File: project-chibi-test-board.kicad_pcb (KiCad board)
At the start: 4 copper layers, 104.1 x 134.6 mm, 221 parts, among them J1 Conn_01x04, J10 Conn_01x02, J11 Conn_01x02, J12 Conn_02x06_Top_Bottom, J13 Conn_02x06_Top_Bottom, J14 Conn_02x06_Top_Bottom, J15 Conn_02x06_Top_Bottom, J16 Conn_01x02, J17 Conn_01x02, J18 Conn_Coaxial, J19 Conn_Coaxial, J2 Conn_Coaxial, J20 Conn_01x03, J21 Conn_01x03, J22 Conn_01x04, J23 USB_B_Micro, J24 Conn_01x06, J25 Conn_01x04, J26 Conn_Coaxial, J27 Conn_Coaxial, J28 Conn_01x03, J29 Conn_01x03, J3 Conn_Coaxial, J30 Conn_01x02, J31 Conn_01x02, J32 Conn_02x06_Top_Bottom, J33 Conn_02x06_Top_Bottom, J34 Conn_02x06_Top_Bottom, J35 Conn_02x06_Top_Bottom, J36 Conn_02x06_Top_Bottom, J37 Conn_02x06_Top_Bottom, J38 Conn_02x06_Top_Bottom, J39 Conn_02x06_Top_Bottom, J4 Conn_01x03, J40 Conn_01x02, J41 Conn_01x02, J42 Conn_Coaxial, J43 Conn_Coaxial, J44 Conn_01x04, J45 Conn_01x03, J46 Conn_01x03, J47 Conn_01x06, J5 Conn_01x03, J6 Conn_02x06_Top_Bottom, J7 Conn_02x06_Top_Bottom, J8 Conn_02x06_Top_Bottom, J9 Conn_01x06, SW1 SW_DIP_x08, SW2 SW_DIP_x08, U1 40 MHz, U10 5M240ZT144C5N, U11 5M1270ZF256C5N, U2 2.048 MHz, U3 5M40ZE64C5N, U4 5M2210ZF256C5N, U5 93LC56BT-OT, U6 5M240ZT144C5N, U7 LM1117-3.3, U8 LM1117-1.8, U9 FT232H, Y1 12 MHz

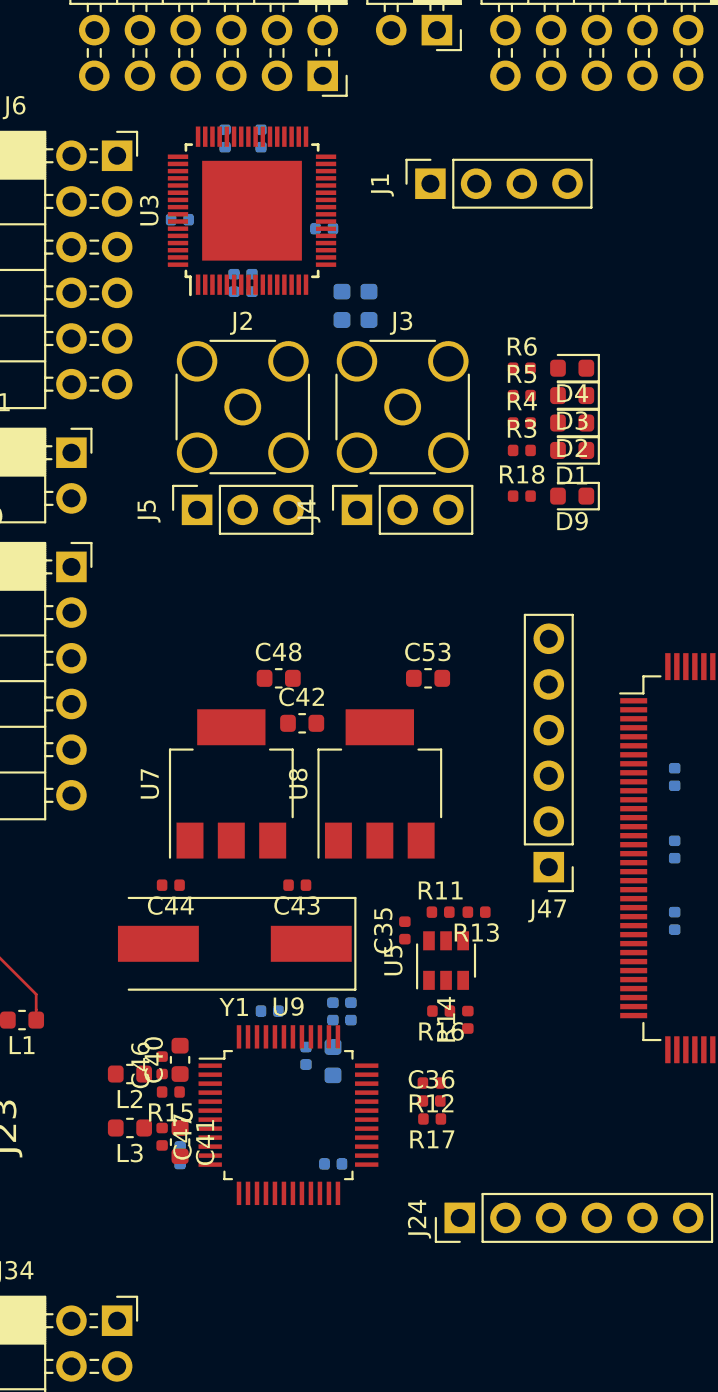
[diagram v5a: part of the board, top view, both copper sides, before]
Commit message: clean up 40z pin ordering
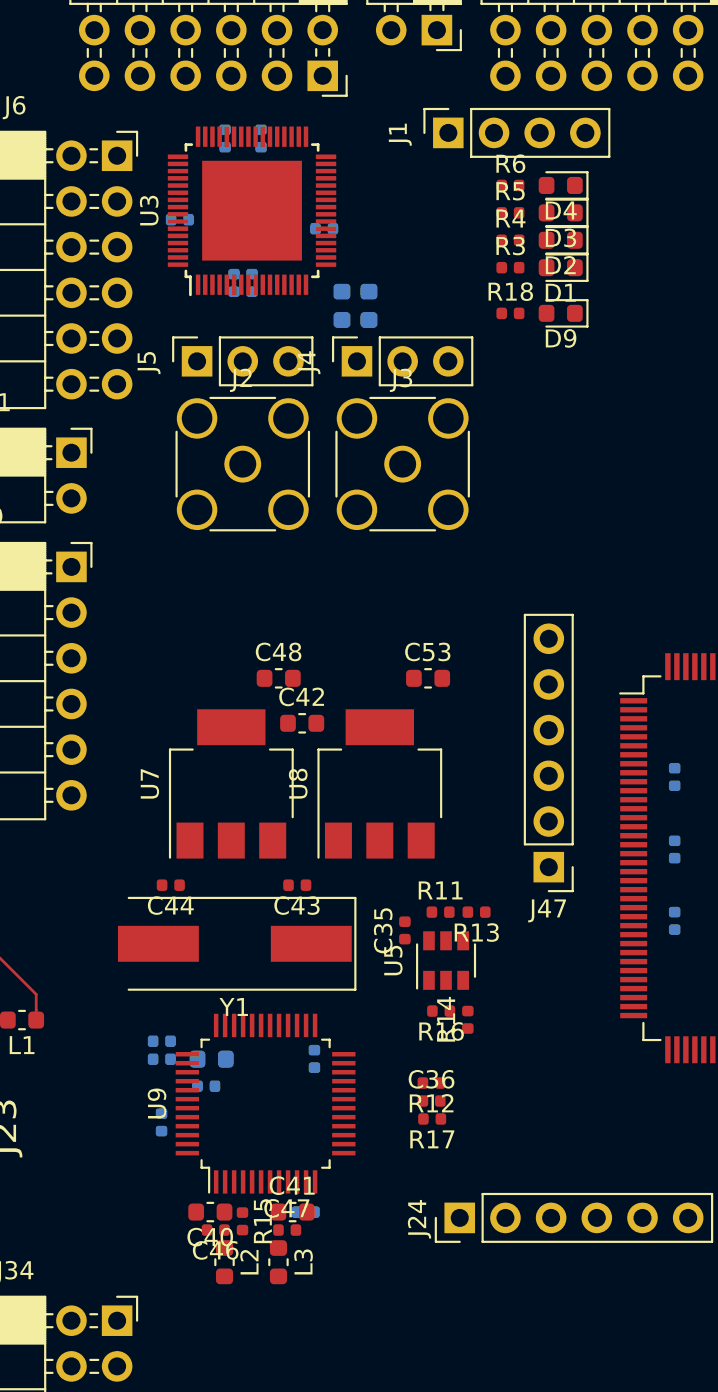
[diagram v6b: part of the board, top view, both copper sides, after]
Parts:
- moved L2 11.7 mm to (69.5, 129.5), turned to 270 degrees
- moved L3 11.1 mm to (72.5, 129.5), turned to 270 degrees
- moved C37 10.6 mm to (66.0, 117.2), turned to 180 degrees
- moved D1 10.2 mm to (88.2, 74.2)
- moved D2 10.2 mm to (88.2, 72.6)
- moved D3 10.2 mm to (88.2, 71.1)
- moved D4 10.2 mm to (88.2, 69.6)
- moved D9 10.2 mm to (88.2, 76.7)
- moved R18 10.2 mm to (85.4, 76.7)
- moved R3 10.2 mm to (85.4, 74.2)
- moved R4 10.2 mm to (85.4, 72.6)
- moved R5 10.2 mm to (85.4, 71.1)
- moved R6 10.2 mm to (85.4, 69.6)
- moved C38 9.88 mm to (66.0, 118.2), turned to 180 degrees
- moved C46 9.63 mm to (69.0, 127.7), turned to 180 degrees
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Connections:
- J6 pad 10: /tgt-4x6/EXPAND0_2 -> /tgt-4x6/EXPAND0_1
- J6 pad 11: /tgt-4x6/EXPAND0_1 -> /tgt-4x6/EXPAND0_4
- J6 pad 2: GND -> +3V3
- J6 pad 3: /tgt-4x6/EXPAND0_7 -> GND
- J6 pad 4: /tgt-4x6/EXPAND0_6 -> GND
- J6 pad 5: /tgt-4x6/EXPAND0_5 -> /tgt-4x6/EXPAND0_7
- J6 pad 6: /tgt-4x6/EXPAND0_4 -> /tgt-4x6/EXPAND0_3
- J6 pad 7: +3V3 -> /tgt-4x6/EXPAND0_6
- J6 pad 8: GND -> /tgt-4x6/EXPAND0_2
- J6 pad 9: /tgt-4x6/EXPAND0_3 -> /tgt-4x6/EXPAND0_5
- J7 pad 10: /tgt-4x6/EXPAND1_2 -> /tgt-4x6/EXPAND1_1
- J7 pad 11: /tgt-4x6/EXPAND1_1 -> /tgt-4x6/EXPAND1_4
- J7 pad 2: GND -> +3V3
- J7 pad 3: /tgt-4x6/EXPAND1_7 -> GND
- J7 pad 4: /tgt-4x6/EXPAND1_6 -> GND
- J7 pad 5: /tgt-4x6/EXPAND1_5 -> /tgt-4x6/EXPAND1_7
- J7 pad 6: /tgt-4x6/EXPAND1_4 -> /tgt-4x6/EXPAND1_3
- J7 pad 7: +3V3 -> /tgt-4x6/EXPAND1_6
- J7 pad 8: GND -> /tgt-4x6/EXPAND1_2
- J7 pad 9: /tgt-4x6/EXPAND1_3 -> /tgt-4x6/EXPAND1_5
- J8 pad 10: /tgt-4x6/EXPAND2_2 -> /tgt-4x6/EXPAND2_1
- J8 pad 11: /tgt-4x6/EXPAND2_1 -> /tgt-4x6/EXPAND2_4
- J8 pad 2: GND -> +3V3
- J8 pad 3: /tgt-4x6/EXPAND2_7 -> GND
- J8 pad 4: /tgt-4x6/EXPAND2_6 -> GND
- J8 pad 5: /tgt-4x6/EXPAND2_5 -> /tgt-4x6/EXPAND2_7
- J8 pad 6: /tgt-4x6/EXPAND2_4 -> /tgt-4x6/EXPAND2_3
- J8 pad 7: +3V3 -> /tgt-4x6/EXPAND2_6
- J8 pad 8: GND -> /tgt-4x6/EXPAND2_2
- J8 pad 9: /tgt-4x6/EXPAND2_3 -> /tgt-4x6/EXPAND2_5
- U3 pad 1: /tgt-4x6/EXPAND0_1 -> /tgt-4x6/EXPAND0_4
- U3 pad 10: /tgt-4x6/EXPAND0_6 -> /tgt-4x6/ADBUS0
- U3 pad 11: /tgt-4x6/EXPAND0_7 -> /tgt-4x6/ADBUS1
- U3 pad 12: /tgt-4x6/EXPAND1_0 -> /tgt-4x6/ADBUS2
- U3 pad 13: /tgt-4x6/EXPAND1_1 -> /tgt-4x6/ADBUS3
- U3 pad 18: /tgt-4x6/EXPAND1_5 -> /tgt-4x6/ADBUS7
- U3 pad 19: /tgt-4x6/EXPAND1_4 -> /tgt-4x6/ADBUS6
- U3 pad 2: /tgt-4x6/EXPAND0_2 -> /tgt-4x6/EXPAND3_3
- U3 pad 20: /tgt-4x6/EXPAND1_3 -> /tgt-4x6/ADBUS5
- U3 pad 21: /tgt-4x6/EXPAND1_2 -> /tgt-4x6/ADBUS4
- U3 pad 22: /tgt-4x6/EXPAND2_0 -> /tgt-4x6/ACBUS2
- U3 pad 24: /tgt-4x6/EXPAND1_7 -> /tgt-4x6/ACBUS1
- U3 pad 25: /tgt-4x6/EXPAND1_6 -> /tgt-4x6/ACBUS0
- U3 pad 26: /tgt-4x6/EXPAND2_2 -> /tgt-4x6/ACBUS4
- U3 pad 27: /tgt-4x6/EXPAND2_1 -> /tgt-4x6/ACBUS3
- U3 pad 3: /tgt-4x6/EXPAND0_3 -> /tgt-4x6/EXPAND3_2
- U3 pad 30: /tgt-4x6/EXPAND2_4 -> /tgt-4x6/ACBUS6
- U3 pad 31: /tgt-4x6/EXPAND2_3 -> /tgt-4x6/ACBUS5
- U3 pad 32: /tgt-4x6/EXPAND2_6 -> Net-(U3-Pad32)
- U3 pad 33: /tgt-4x6/EXPAND2_5 -> Net-(R3-Pad1)
- U3 pad 34: /tgt-4x6/ADBUS0 -> Net-(R6-Pad1)
- U3 pad 35: Net-(R6-Pad1) -> Net-(R5-Pad1)
- U3 pad 36: Net-(R5-Pad1) -> Net-(R4-Pad1)
- U3 pad 37: Net-(R4-Pad1) -> /tgt-4x6/EXPAND2_7
- U3 pad 38: Net-(R3-Pad1) -> /tgt-4x6/EXPAND2_3
- U3 pad 4: /tgt-4x6/EXPAND0_4 -> /tgt-4x6/EXPAND3_1
- U3 pad 43: /tgt-4x6/EXPAND2_7 -> /tgt-4x6/EXPAND2_6
- U3 pad 44: Net-(U3-Pad44) -> /tgt-4x6/EXPAND2_2
- U3 pad 45: /tgt-4x6/EXPAND3_3 -> /tgt-4x6/EXPAND2_5
- U3 pad 46: /tgt-4x6/EXPAND3_2 -> /tgt-4x6/EXPAND2_1
- U3 pad 47: /tgt-4x6/EXPAND3_1 -> /tgt-4x6/EXPAND2_4
- U3 pad 48: /tgt-4x6/EXPAND3_0 -> /tgt-4x6/EXPAND2_0
- U3 pad 49: /tgt-4x6/ACBUS5 -> /tgt-4x6/EXPAND1_3
- U3 pad 5: /tgt-4x6/EXPAND0_5 -> /tgt-4x6/EXPAND3_0
- U3 pad 50: /tgt-4x6/ACBUS6 -> /tgt-4x6/EXPAND1_7
- U3 pad 51: /tgt-4x6/ACBUS2 -> /tgt-4x6/EXPAND1_2
- U3 pad 52: /tgt-4x6/ACBUS3 -> /tgt-4x6/EXPAND1_6
- U3 pad 53: /tgt-4x6/ACBUS4 -> /tgt-4x6/EXPAND1_1
- U3 pad 54: /tgt-4x6/ACBUS0 -> /tgt-4x6/EXPAND1_5
- U3 pad 55: /tgt-4x6/ACBUS1 -> /tgt-4x6/EXPAND1_0
- U3 pad 56: /tgt-4x6/ADBUS4 -> /tgt-4x6/EXPAND1_4
- U3 pad 58: /tgt-4x6/ADBUS5 -> /tgt-4x6/EXPAND0_3
- U3 pad 59: /tgt-4x6/ADBUS6 -> /tgt-4x6/EXPAND0_7
- U3 pad 60: /tgt-4x6/ADBUS7 -> /tgt-4x6/EXPAND0_2
- U3 pad 61: /tgt-4x6/ADBUS1 -> /tgt-4x6/EXPAND0_6
- U3 pad 62: /tgt-4x6/ADBUS2 -> /tgt-4x6/EXPAND0_1
- U3 pad 63: /tgt-4x6/ADBUS3 -> /tgt-4x6/EXPAND0_5

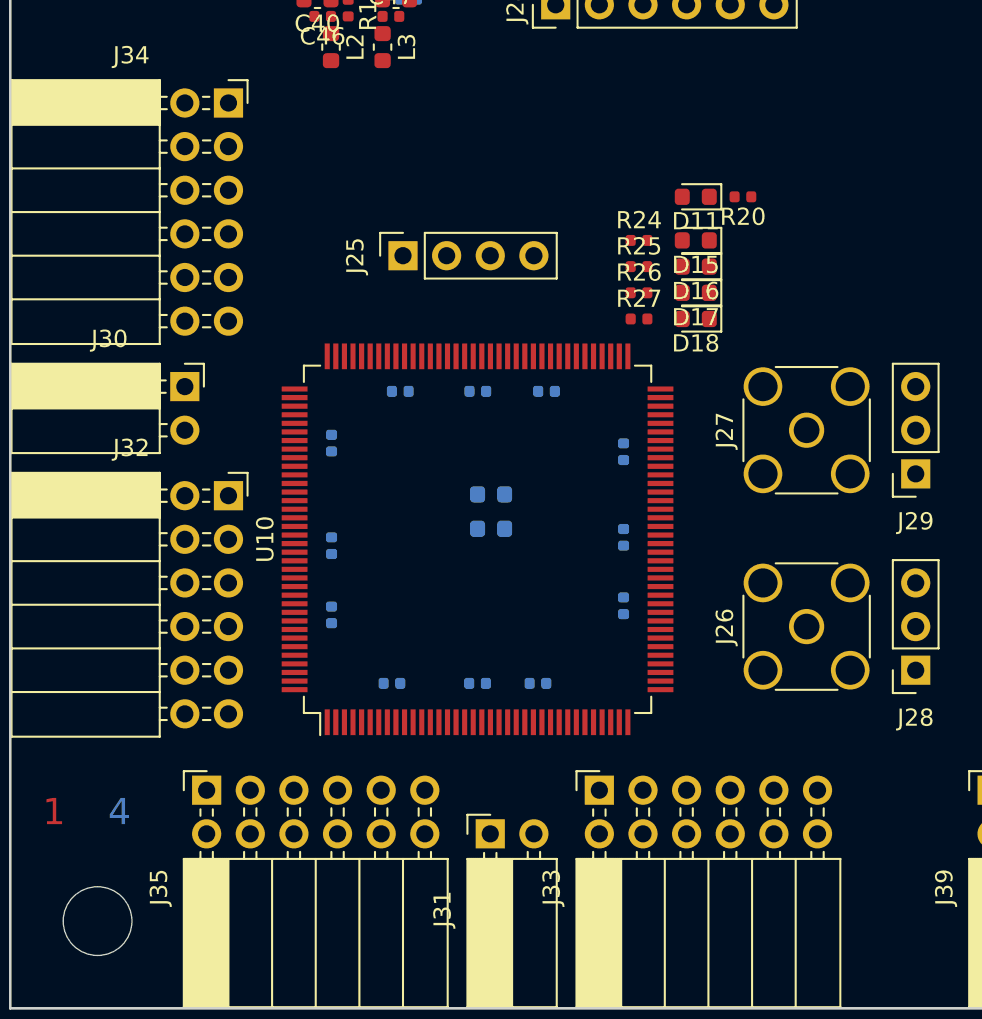
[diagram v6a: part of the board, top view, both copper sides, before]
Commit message: clean up 240z pin ordering
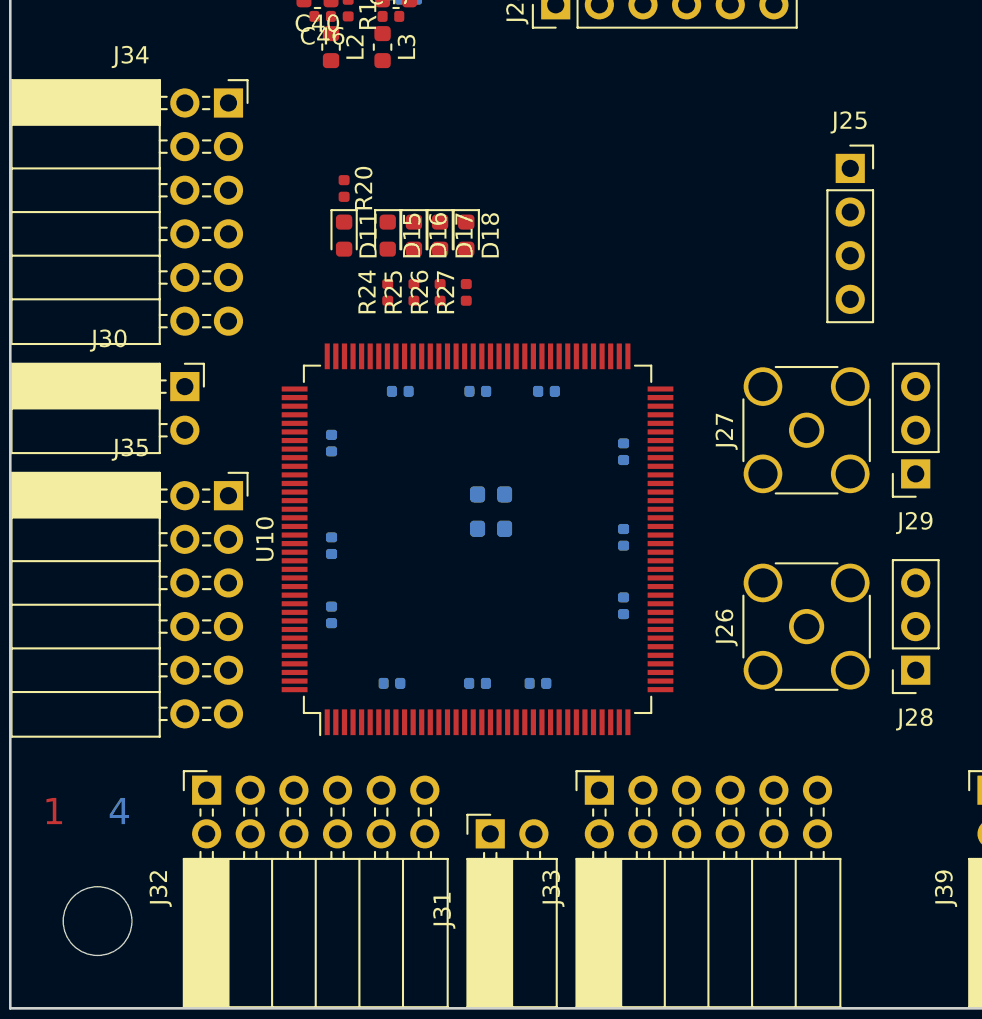
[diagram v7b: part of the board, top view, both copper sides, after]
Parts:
- moved J25 26.5 mm to (99.7, 136.5), turned to 0 degrees
- moved R20 23.2 mm to (70.2, 137.7), turned to 270 degrees
- moved D11 20.6 mm to (70.2, 140.4), turned to 270 degrees
- moved D15 17.9 mm to (72.8, 140.4), turned to 270 degrees
- moved J32 17.2 mm to (62.2, 172.7), turned to 90 degrees
- moved J35 17.2 mm to (63.5, 155.6), turned to 0 degrees
- moved D16 16.5 mm to (74.3, 140.4), turned to 270 degrees
- moved D17 15.3 mm to (75.8, 140.4), turned to 270 degrees
- moved R24 14.9 mm to (72.8, 143.7), turned to 90 degrees
- moved D18 14.2 mm to (77.3, 140.4), turned to 270 degrees
- moved R25 13.2 mm to (74.3, 143.7), turned to 90 degrees
- moved R26 11.6 mm to (75.8, 143.7), turned to 90 degrees
- moved R27 10.2 mm to (77.3, 143.7), turned to 90 degrees
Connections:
- J32 pad 10: /tgt-7x12/EXPAND0_2 -> /tgt-7x12/EXPAND0_1
- J32 pad 11: /tgt-7x12/EXPAND0_1 -> /tgt-7x12/EXPAND0_4
- J32 pad 2: GND -> +3V3
- J32 pad 3: /tgt-7x12/EXPAND0_7 -> GND
- J32 pad 4: /tgt-7x12/EXPAND0_6 -> GND
- J32 pad 5: /tgt-7x12/EXPAND0_5 -> /tgt-7x12/EXPAND0_7
- J32 pad 6: /tgt-7x12/EXPAND0_4 -> /tgt-7x12/EXPAND0_3
- J32 pad 7: +3V3 -> /tgt-7x12/EXPAND0_6
- J32 pad 8: GND -> /tgt-7x12/EXPAND0_2
- J32 pad 9: /tgt-7x12/EXPAND0_3 -> /tgt-7x12/EXPAND0_5
- J33 pad 10: /tgt-7x12/EXPAND1_2 -> /tgt-7x12/EXPAND1_1
- J33 pad 11: /tgt-7x12/EXPAND1_1 -> /tgt-7x12/EXPAND1_4
- J33 pad 2: GND -> +3V3
- J33 pad 3: /tgt-7x12/EXPAND1_7 -> GND
- J33 pad 4: /tgt-7x12/EXPAND1_6 -> GND
- J33 pad 5: /tgt-7x12/EXPAND1_5 -> /tgt-7x12/EXPAND1_7
- J33 pad 6: /tgt-7x12/EXPAND1_4 -> /tgt-7x12/EXPAND1_3
- J33 pad 7: +3V3 -> /tgt-7x12/EXPAND1_6
- J33 pad 8: GND -> /tgt-7x12/EXPAND1_2
- J33 pad 9: /tgt-7x12/EXPAND1_3 -> /tgt-7x12/EXPAND1_5
- J34 pad 10: /tgt-7x12/EXPAND2_2 -> /tgt-7x12/EXPAND2_1
- J34 pad 11: /tgt-7x12/EXPAND2_1 -> /tgt-7x12/EXPAND2_4
- J34 pad 2: GND -> +3V3
- J34 pad 3: /tgt-7x12/EXPAND2_7 -> GND
- J34 pad 4: /tgt-7x12/EXPAND2_6 -> GND
- J34 pad 5: /tgt-7x12/EXPAND2_5 -> /tgt-7x12/EXPAND2_7
- J34 pad 6: /tgt-7x12/EXPAND2_4 -> /tgt-7x12/EXPAND2_3
- J34 pad 7: +3V3 -> /tgt-7x12/EXPAND2_6
- J34 pad 8: GND -> /tgt-7x12/EXPAND2_2
- J34 pad 9: /tgt-7x12/EXPAND2_3 -> /tgt-7x12/EXPAND2_5
- J35 pad 10: /tgt-7x12/EXPAND3_2 -> /tgt-7x12/EXPAND3_1
- J35 pad 11: /tgt-7x12/EXPAND3_1 -> /tgt-7x12/EXPAND3_4
- J35 pad 2: GND -> +3V3
- J35 pad 3: /tgt-7x12/EXPAND3_7 -> GND
- J35 pad 4: /tgt-7x12/EXPAND3_6 -> GND
- J35 pad 5: /tgt-7x12/EXPAND3_5 -> /tgt-7x12/EXPAND3_7
- J35 pad 6: /tgt-7x12/EXPAND3_4 -> /tgt-7x12/EXPAND3_3
- J35 pad 7: +3V3 -> /tgt-7x12/EXPAND3_6
- J35 pad 8: GND -> /tgt-7x12/EXPAND3_2
- J35 pad 9: /tgt-7x12/EXPAND3_3 -> /tgt-7x12/EXPAND3_5
- U10 pad 1: /tgt-7x12/EXPAND1_2 -> /tgt-7x12/EXPAND0_7
- U10 pad 102: /tgt-7x12/EXPAND2_6 -> /tgt-7x12/EXPAND2_3
- U10 pad 103: /tgt-7x12/EXPAND2_5 -> /tgt-7x12/EXPAND2_6
- U10 pad 104: /tgt-7x12/EXPAND2_4 -> /tgt-7x12/EXPAND2_2
- U10 pad 105: /tgt-7x12/EXPAND2_3 -> /tgt-7x12/EXPAND2_5
- U10 pad 106: /tgt-7x12/EXPAND2_2 -> /tgt-7x12/EXPAND2_1
- U10 pad 107: /tgt-7x12/EXPAND2_1 -> /tgt-7x12/EXPAND2_4
- U10 pad 109: /tgt-7x12/ACBUS4 -> Net-(U10-Pad109)
- U10 pad 11: /tgt-7x12/EXPAND0_4 -> /tgt-7x12/EXPAND0_0
- U10 pad 110: /tgt-7x12/ACBUS5 -> Net-(U10-Pad110)
- U10 pad 111: /tgt-7x12/ACBUS6 -> Net-(U10-Pad111)
- U10 pad 112: /tgt-7x12/ACBUS2 -> Net-(U10-Pad112)
- U10 pad 113: /tgt-7x12/ACBUS3 -> Net-(U10-Pad113)
- U10 pad 114: /tgt-7x12/ACBUS0 -> Net-(U10-Pad114)
- U10 pad 117: /tgt-7x12/ACBUS1 -> Net-(U10-Pad117)
- U10 pad 118: /tgt-7x12/ADBUS5 -> Net-(U10-Pad118)
- U10 pad 119: /tgt-7x12/ADBUS6 -> Net-(U10-Pad119)
- U10 pad 12: /tgt-7x12/EXPAND0_5 -> Net-(U10-Pad12)
- U10 pad 120: /tgt-7x12/ADBUS7 -> Net-(U10-Pad120)
- U10 pad 121: /tgt-7x12/ADBUS1 -> Net-(U10-Pad121)
- U10 pad 122: /tgt-7x12/ADBUS2 -> Net-(U10-Pad122)
- U10 pad 123: /tgt-7x12/ADBUS3 -> Net-(U10-Pad123)
- U10 pad 124: /tgt-7x12/ADBUS4 -> Net-(U10-Pad124)
- U10 pad 125: Net-(R25-Pad1) -> Net-(U10-Pad125)
- U10 pad 127: Net-(R26-Pad1) -> Net-(U10-Pad127)
- U10 pad 129: Net-(R27-Pad1) -> Net-(U10-Pad129)
- U10 pad 13: /tgt-7x12/EXPAND0_6 -> Net-(U10-Pad13)
- U10 pad 130: /tgt-7x12/ADBUS0 -> Net-(U10-Pad130)
- U10 pad 131: /tgt-7x12/EXPAND3_7 -> Net-(U10-Pad131)
- U10 pad 134: Net-(R24-Pad1) -> /tgt-7x12/EXPAND3_7
- U10 pad 138: /tgt-7x12/EXPAND3_5 -> /tgt-7x12/EXPAND3_3
- U10 pad 14: /tgt-7x12/EXPAND0_7 -> Net-(U10-Pad14)
- U10 pad 140: /tgt-7x12/EXPAND3_3 -> /tgt-7x12/EXPAND3_2
- U10 pad 141: /tgt-7x12/EXPAND3_4 -> /tgt-7x12/EXPAND3_1
- U10 pad 142: /tgt-7x12/EXPAND3_1 -> /tgt-7x12/EXPAND3_5
- U10 pad 143: /tgt-7x12/EXPAND3_2 -> /tgt-7x12/EXPAND3_0
- U10 pad 144: /tgt-7x12/EXPAND3_0 -> /tgt-7x12/EXPAND3_4
- U10 pad 2: /tgt-7x12/EXPAND1_0 -> /tgt-7x12/EXPAND0_3
- U10 pad 3: /tgt-7x12/EXPAND1_1 -> /tgt-7x12/EXPAND0_6
- U10 pad 31: /tgt-7x12/EXPAND1_4 -> /tgt-7x12/EXPAND1_3
- U10 pad 32: /tgt-7x12/EXPAND1_3 -> /tgt-7x12/EXPAND1_7
- U10 pad 37: /tgt-7x12/EXPAND1_7 -> /tgt-7x12/EXPAND1_6
- U10 pad 38: /tgt-7x12/EXPAND1_6 -> /tgt-7x12/EXPAND1_2
- U10 pad 4: /tgt-7x12/EXPAND0_0 -> /tgt-7x12/EXPAND0_2
- U10 pad 40: Net-(U10-Pad40) -> /tgt-7x12/EXPAND1_1
- U10 pad 41: Net-(U10-Pad41) -> /tgt-7x12/EXPAND1_4
- U10 pad 42: Net-(U10-Pad42) -> /tgt-7x12/EXPAND1_0
- U10 pad 6: /tgt-7x12/EXPAND0_2 -> /tgt-7x12/EXPAND0_5
- U10 pad 7: /tgt-7x12/EXPAND0_3 -> /tgt-7x12/EXPAND0_4
- U10 pad 71: Net-(U10-Pad71) -> /tgt-7x12/ACBUS6
- U10 pad 72: Net-(U10-Pad72) -> /tgt-7x12/ACBUS5
- U10 pad 73: Net-(U10-Pad73) -> /tgt-7x12/ACBUS4
- U10 pad 74: Net-(U10-Pad74) -> /tgt-7x12/ACBUS3
- U10 pad 75: Net-(U10-Pad75) -> /tgt-7x12/ACBUS2
- U10 pad 76: Net-(U10-Pad76) -> /tgt-7x12/ACBUS1
- U10 pad 77: Net-(U10-Pad77) -> /tgt-7x12/ACBUS0
- U10 pad 78: Net-(U10-Pad78) -> /tgt-7x12/ADBUS7
- U10 pad 79: Net-(U10-Pad79) -> /tgt-7x12/ADBUS6
- U10 pad 80: Net-(U10-Pad80) -> /tgt-7x12/ADBUS5
- U10 pad 81: Net-(U10-Pad81) -> /tgt-7x12/ADBUS4
- U10 pad 84: Net-(U10-Pad84) -> /tgt-7x12/ADBUS3
- U10 pad 85: Net-(U10-Pad85) -> /tgt-7x12/ADBUS2
- U10 pad 86: Net-(U10-Pad86) -> /tgt-7x12/ADBUS1
- U10 pad 87: Net-(U10-Pad87) -> /tgt-7x12/ADBUS0
- U10 pad 95: Net-(U10-Pad95) -> Net-(R27-Pad1)
- U10 pad 96: Net-(U10-Pad96) -> Net-(R26-Pad1)
- U10 pad 97: Net-(U10-Pad97) -> Net-(R25-Pad1)
- U10 pad 98: Net-(U10-Pad98) -> Net-(R24-Pad1)
